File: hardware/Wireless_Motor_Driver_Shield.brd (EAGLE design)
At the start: 59.7 x 53.3 mm, 96 parts, among them J1 5.5x2.1mm Barrel, Q1 MOSFET-NCHANNELBSS138, Q2 MOSFET-NCHANNELBSS138, Q3 MMBT2222A, Q4 DMG2307L, Q5 DMG2307L, Q6 DMG2307L, U1 XBEE-1XBEE-1_LOCK, U2 ARDUINO, U3 TB6612FNG

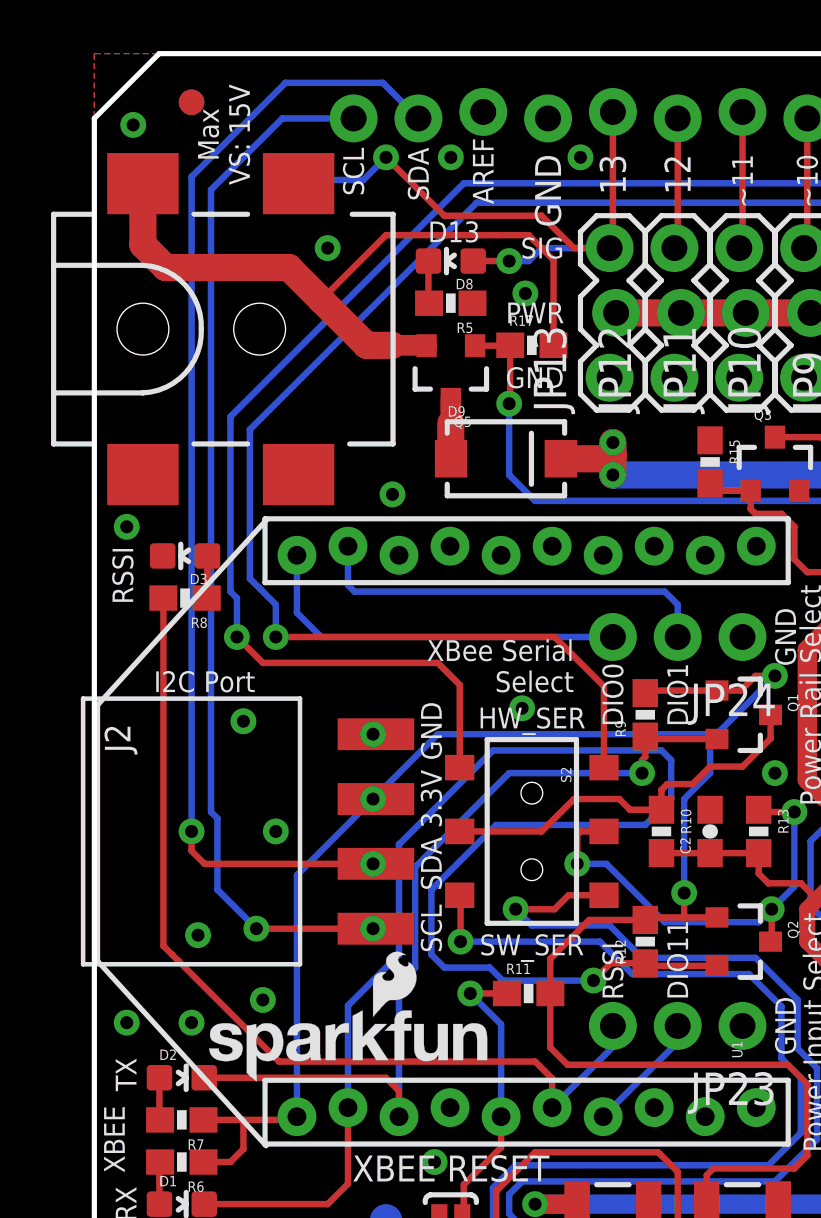
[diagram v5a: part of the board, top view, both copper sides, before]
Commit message: Added staking vias to barrel jack. Added header PTH for VS.
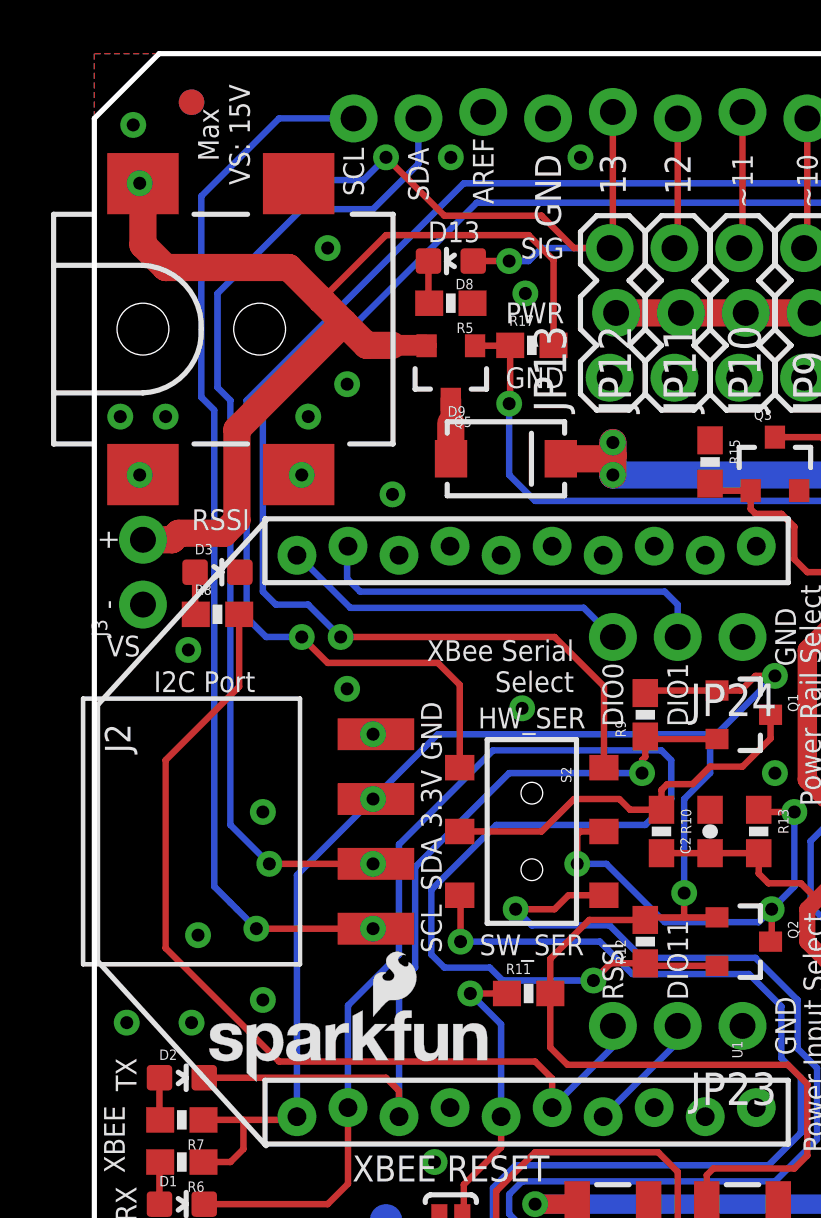
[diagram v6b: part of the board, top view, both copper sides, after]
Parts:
- added J3: (no value), SparkFun-Connectors:1X02_NO_SILK
- moved D3 1.42 mm to (4.83, 33.0), turned to 270 degrees
- moved R8 1.42 mm to (4.83, 31.4), turned to 0 degrees
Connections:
- net GND: now also J3.1
- net N$10: now also J3.2
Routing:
- net N$10: track 29.1 -> 42.7 mm, vias 0 -> 1
- net SDA: track 44.8 -> 39.1 mm
- net DIO0: track 15.0 -> 13.7 mm
- net D1/TXO: track 79.9 -> 78.7 mm
- net D0/RXI: track 85.7 -> 84.6 mm
- net RSSI: track 36.3 -> 36.9 mm
